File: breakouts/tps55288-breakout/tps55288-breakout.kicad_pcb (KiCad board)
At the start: 2 copper layers, 1 part, among them U1 TPS55288RPMR

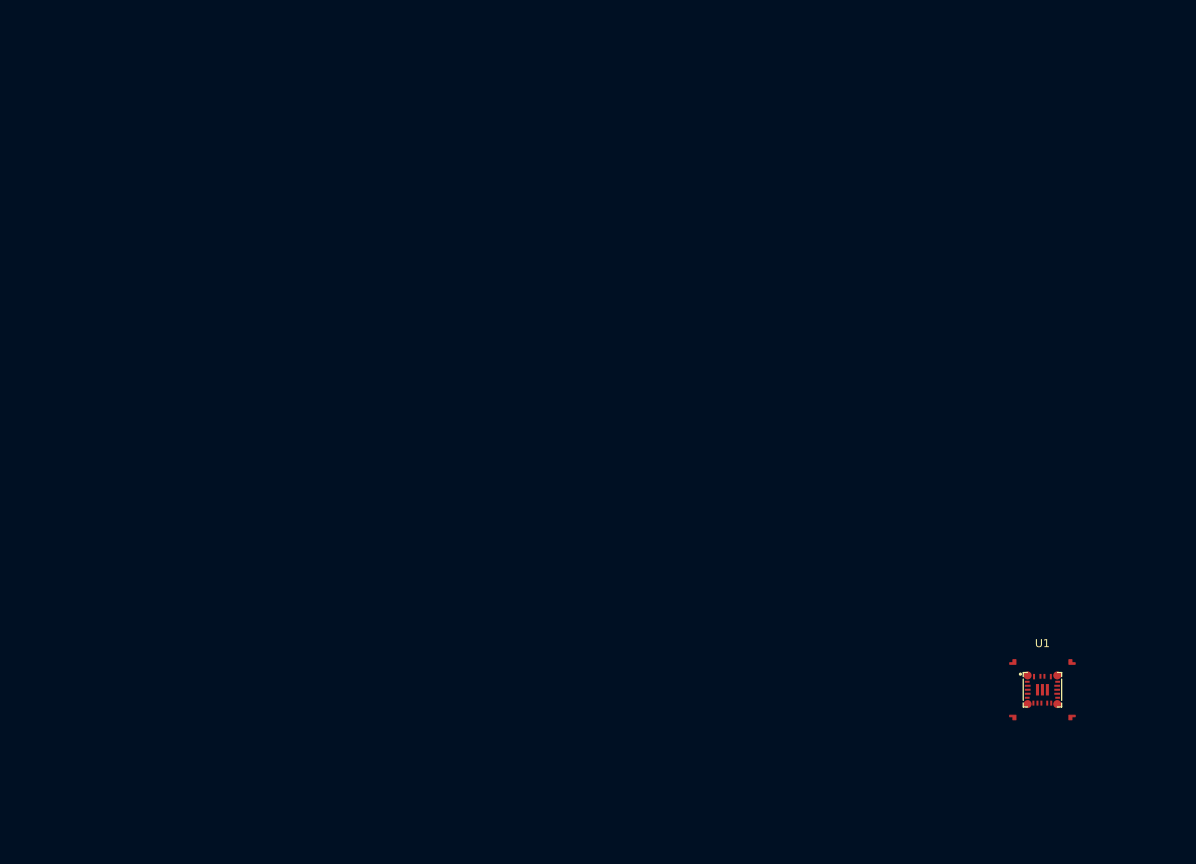
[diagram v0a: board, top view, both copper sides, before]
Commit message: finish schematic equations... by using the calculator that TI provides
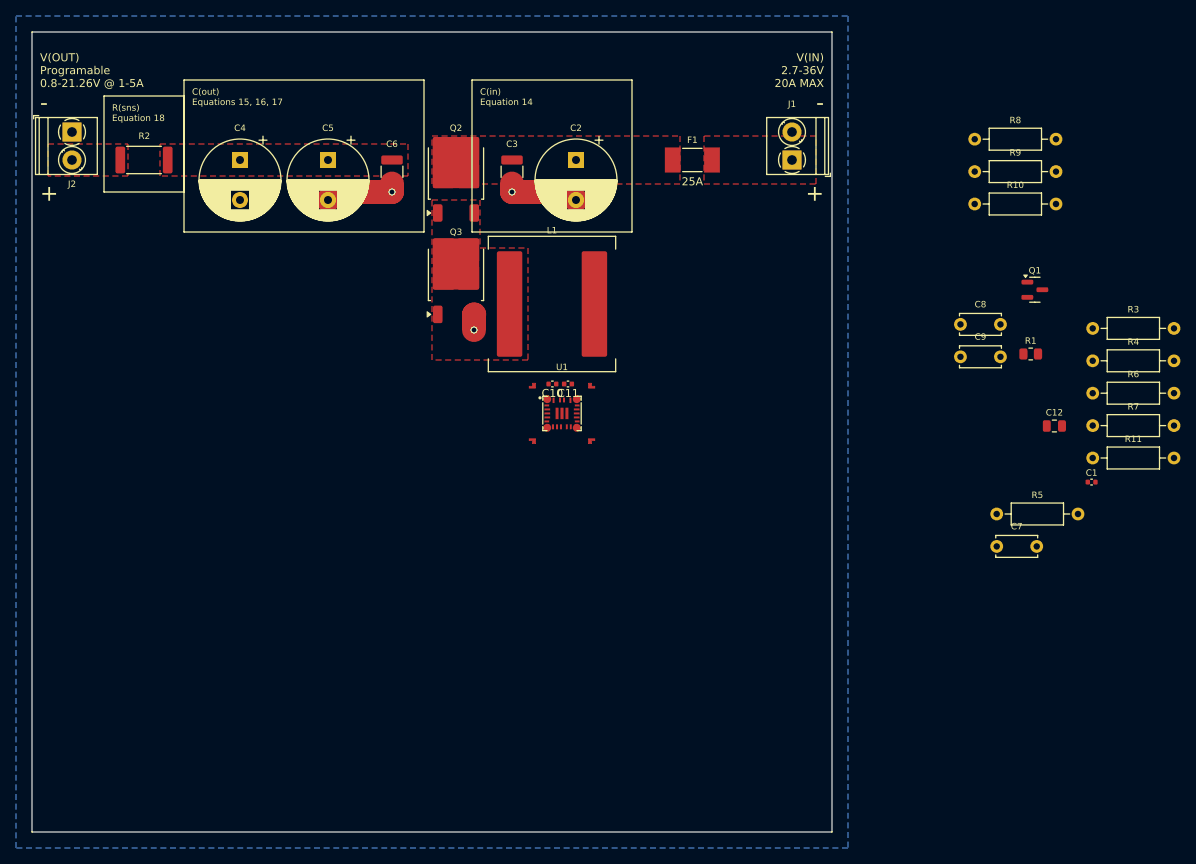
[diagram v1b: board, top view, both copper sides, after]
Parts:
- added C1: 0.1u, Capacitor_SMD:C_0402_1005Metric, F.Cu at (147.4, 71.3)
- added C10: 0.1u, Capacitor_SMD:C_0402_1005Metric, F.Cu at (80.0, 59.0)
- added C11: 0.1u, Capacitor_SMD:C_0402_1005Metric, F.Cu at (82.0, 59.0)
- added C12: 4.7u, Capacitor_SMD:C_0805_2012Metric, F.Cu at (142.8, 64.2)
- added C2: 330u, Capacitor_THT:CP_Radial_D10.0mm_P5.00mm, F.Cu at (83.0, 31.0)
- added C3: 10u, Capacitor_SMD:C_1210_3225Metric, F.Cu at (75.0, 32.5)
- added C4: 330u, Capacitor_THT:CP_Radial_D10.0mm_P5.00mm, F.Cu at (41.0, 31.0)
- added C5: 330u, Capacitor_THT:CP_Radial_D10.0mm_P5.00mm, F.Cu at (52.0, 31.0)
- added C6: 10u, Capacitor_SMD:C_1210_3225Metric, F.Cu at (60.0, 32.5)
- added C7: 10n, Capacitor_THT:C_Disc_D5.0mm_W2.5mm_P5.00mm, F.Cu at (135.6, 79.3)
- added C8: 150p, Capacitor_THT:C_Disc_D5.0mm_W2.5mm_P5.00mm, F.Cu at (131.1, 51.5)
- added C9: 15n, Capacitor_THT:C_Disc_D5.0mm_W2.5mm_P5.00mm, F.Cu at (131.1, 55.6)
- added F1: 25A, Fuse:Fuse_Littelfuse-NANO2-451_453, F.Cu at (97.5, 31.0)
- added J1: Screw_Terminal_01x02, TerminalBlock_Phoenix:TerminalBlock_Phoenix_PT-1,5-2-3.5-H_1x02_P3.50mm_Horizontal, F.Cu at (110.0, 31.0)
- added J2: Screw_Terminal_01x02, TerminalBlock_Phoenix:TerminalBlock_Phoenix_PT-1,5-2-3.5-H_1x02_P3.50mm_Horizontal, F.Cu at (20.0, 27.5)
- added L1: 4.7u, Inductor_SMD:L_Coilcraft_XAL1510-682, F.Cu at (80.0, 49.0)
- added Q1: 2N7002K, Package_TO_SOT_SMD:SOT-23, F.Cu at (140.4, 47.2)
- added Q2: QM6006D, Package_TO_SOT_SMD:TO-252-2, F.Cu at (68.0, 32.6)
- added Q3: QM6006D, Package_TO_SOT_SMD:TO-252-2, F.Cu at (68.0, 45.3)
- added R1: 10k, Resistor_SMD:R_0805_2012Metric, F.Cu at (139.8, 55.2)
- added R10: 16k, Resistor_THT:R_Axial_DIN0207_L6.3mm_D2.5mm_P10.16mm_Horizontal, F.Cu at (132.8, 36.5)
- added R11: 91k, Resistor_THT:R_Axial_DIN0207_L6.3mm_D2.5mm_P10.16mm_Horizontal, F.Cu at (147.6, 68.2)
- added R2: 10m, Resistor_SMD:R_2512_6332Metric, F.Cu at (29.0, 31.0)
- added R3: 4.3k, Resistor_THT:R_Axial_DIN0207_L6.3mm_D2.5mm_P10.16mm_Horizontal, F.Cu at (147.6, 52.0)
- added R4: 1k, Resistor_THT:R_Axial_DIN0207_L6.3mm_D2.5mm_P10.16mm_Horizontal, F.Cu at (147.6, 56.1)
- added R5: 47k, Resistor_THT:R_Axial_DIN0207_L6.3mm_D2.5mm_P10.16mm_Horizontal, F.Cu at (135.6, 75.2)
- added R6: 100k, Resistor_THT:R_Axial_DIN0207_L6.3mm_D2.5mm_P10.16mm_Horizontal, F.Cu at (147.6, 60.1)
- added R7: 1k, Resistor_THT:R_Axial_DIN0207_L6.3mm_D2.5mm_P10.16mm_Horizontal, F.Cu at (147.6, 64.2)
- added R8: 0, Resistor_THT:R_Axial_DIN0207_L6.3mm_D2.5mm_P10.16mm_Horizontal, F.Cu at (132.8, 28.4)
- added R9: 20k, Resistor_THT:R_Axial_DIN0207_L6.3mm_D2.5mm_P10.16mm_Horizontal, F.Cu at (132.8, 32.5)
- U1: footprint LCSC:VQFN-HR-26_L4.0-W3.5_TPS55288RPMR -> LCSC-powercoop:VQFN-HR-26_L4.0-W3.5_TPS55288RPMR
- moved U1 69.3 mm to (81.2, 62.7)
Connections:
- U1 pad 1: unconnected-(U1-DR1L-Pad1) -> /DR1L
- U1 pad 10: unconnected-(U1-AGND-Pad10) -> /AGND
- U1 pad 11: unconnected-(U1-VOUT-Pad11) -> /VOUT
- U1 pad 12: unconnected-(U1-ISP-Pad12) -> /VOUT
- U1 pad 13: unconnected-(U1-ISN-Pad13) -> /ISN
- U1 pad 14: unconnected-(U1-FB/INT-Pad14) -> /FB/INT
- U1 pad 15: unconnected-(U1-MODE-Pad15) -> /MODE
- U1 pad 16: unconnected-(U1-CDC-Pad16) -> /CDC
- U1 pad 17: unconnected-(U1-ILIM-Pad17) -> /ILIM
- U1 pad 18: unconnected-(U1-COMP-Pad18) -> /COMP
- U1 pad 19: unconnected-(U1-VCC-Pad19) -> /VCC
- U1 pad 2: unconnected-(U1-DR1H-Pad2) -> /DR1H
- U1 pad 20: unconnected-(U1-BOOT2-Pad20) -> /BOOT2
- U1 pad 21: unconnected-(U1-SW2-Pad21) -> /SW2
- U1 pad 22: unconnected-(U1-BOOT1-Pad22) -> /BOOT1
- U1 pad 23: unconnected-(U1-SW1-Pad23) -> /SW1
- U1 pad 24: unconnected-(U1-PGND-Pad24) -> GND
- U1 pad 25: unconnected-(U1-SW2-Pad25) -> /SW2
- U1 pad 26: unconnected-(U1-VOUT-Pad26) -> /VOUT
- U1 pad 3: unconnected-(U1-VIN-Pad3) -> /VIN
- U1 pad 4: unconnected-(U1-EN/UVLO-Pad4) -> /EN/UVLO
- U1 pad 5: unconnected-(U1-SCL-Pad5) -> /SCL
- U1 pad 6: unconnected-(U1-SDA-Pad6) -> /SDA
- U1 pad 7: unconnected-(U1-DITH/SYNC-Pad7) -> /DITH/SYNC
- U1 pad 8: unconnected-(U1-FSW-Pad8) -> /FSW
- U1 pad 9: unconnected-(U1-PGND-Pad9) -> GND
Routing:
- net GND: track 0.00 -> 20.9 mm, vias 0 -> 3
- added copper zone on F.Cu, net /ISN
- added copper zone on F.Cu, net /SW1
- added copper zone on F.Cu, net /VIN
- added copper zone on F.Cu, net /VOUT
- added copper zone on B.Cu, net GND
- added copper zone on F.Cu, net Net-(J1-Pin_1)
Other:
- board outline added: 100 x 100 mm
- board text added: "+"
- board text added: "-"
- board text added: "C(in) Equation 14"
- board text added: "C(out) Equations 15, 16, 17"
- board text added: "R(sns) Equation 18"
- board text added: "V(IN) 2.7-36V 20A MAX"
- board text added: "V(OUT) Programable 0.8-21.26V @ 1-5A"

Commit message: first pass at full-featured TPS55288 breakout board
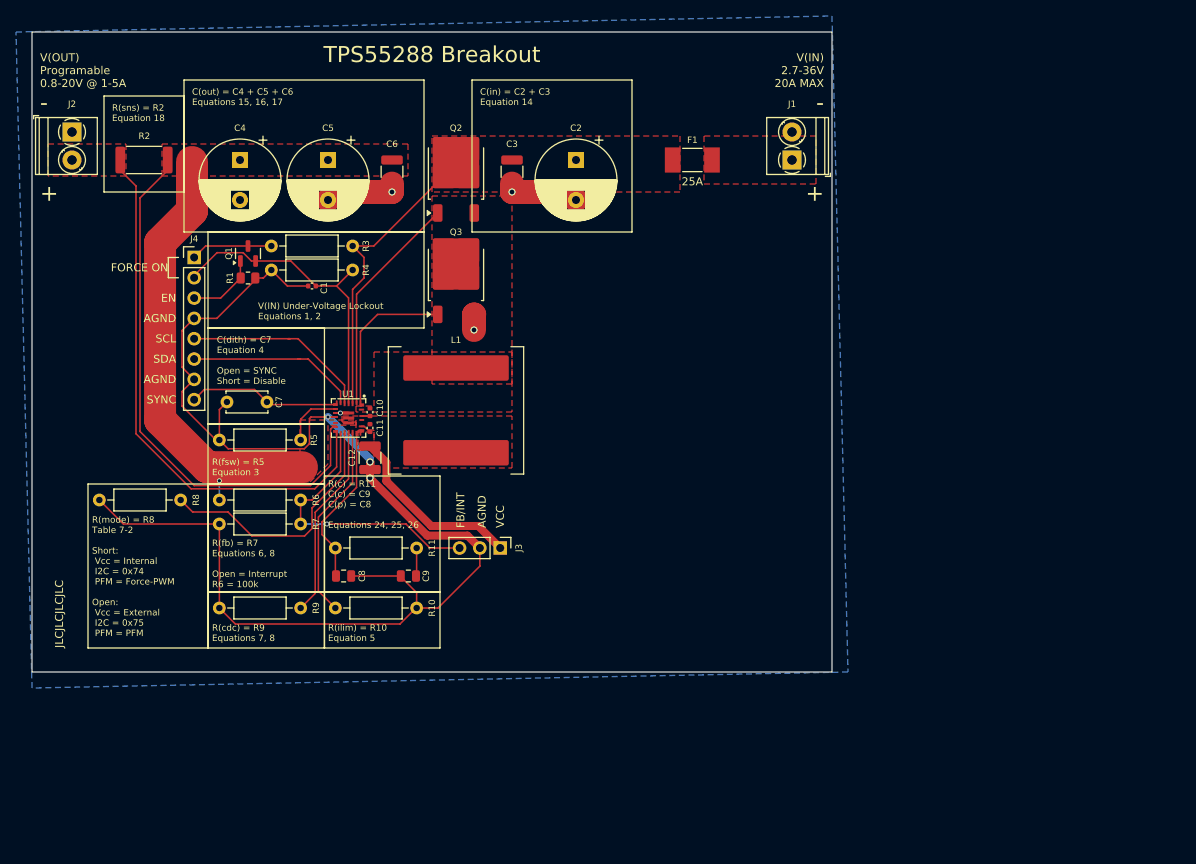
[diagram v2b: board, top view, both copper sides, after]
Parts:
- added J3: Conn_01x10_Pin, Connector_PinHeader_2.54mm:PinHeader_1x03_P2.54mm_Vertical, F.Cu at (73.5, 79.5)
- added J4: Conn_01x06_Pin, Connector_PinHeader_2.54mm:PinHeader_1x08_P2.54mm_Vertical, F.Cu at (35.3, 43.2)
- C12: value 4.7u -> 10u; footprint Capacitor_SMD:C_0805_2012Metric -> Capacitor_SMD:C_1210_3225Metric
- C2: value 330u -> 100u
- C8, C9: footprint Capacitor_THT:C_Disc_D5.0mm_W2.5mm_P5.00mm -> Capacitor_SMD:C_0805_2012Metric
- moved R6 110.0 mm to (38.4, 73.5)
- moved R8 109.0 mm to (33.6, 73.5), turned to 180 degrees
- moved C1 100.5 mm to (50.0, 46.8)
- moved R9 100.4 mm to (48.6, 87.0), turned to 180 degrees
- moved R7 99.8 mm to (48.6, 76.5), turned to 180 degrees
- moved Q1 98.5 mm to (42.0, 42.7), turned to 90 degrees
- moved R1 98.3 mm to (42.0, 45.8), turned to 180 degrees
- moved C7 97.9 mm to (39.4, 61.2)
- moved R11 95.3 mm to (52.9, 79.5)
- moved R10 94.5 mm to (52.9, 87.0)
- moved R4 93.2 mm to (55.1, 44.8), turned to 180 degrees
- moved R3 93.1 mm to (55.1, 41.8), turned to 180 degrees
- moved R5 87.5 mm to (48.6, 66.0), turned to 180 degrees
- moved C12 85.6 mm to (57.2, 68.2), turned to 90 degrees
- moved C8 83.3 mm to (54.0, 83.0), turned to 180 degrees
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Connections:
- net Net-(Q1-D) renamed /ON
- C7 pad 1: GND -> /AGND
- Q1 pad 2: Net-(Q1-S) -> /EN/UVLO
- R5 pad 2: GND -> /AGND
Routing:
- net /AGND: track 0.00 -> 164.2 mm, vias 0 -> 2
- net /VOUT: track 0.00 -> 124.8 mm, vias 0 -> 1
- net /ISN: track 0.00 -> 68.7 mm
- net /EN/UVLO: track 0.00 -> 38.8 mm
- net /VIN: track 0.00 -> 35.9 mm
- net /FB/INT: track 0.00 -> 35.4 mm, vias 0 -> 1
- net /MODE: track 0.00 -> 32.3 mm
- net /DR1H: track 0.00 -> 27.9 mm
- net /ILIM: track 0.00 -> 24.6 mm
- net /CDC: track 0.00 -> 24.4 mm
- net /SCL: track 0.00 -> 23.8 mm
- net /VCC: track 0.00 -> 22.9 mm
- net /SDA: track 0.00 -> 21.7 mm
- net /COMP: track 0.00 -> 20.4 mm
- net /DR1L: track 0.00 -> 19.5 mm
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- added copper zone on F.Cu, net /SW2
- added copper zone on F.Cu, net /VCC
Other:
- board size 100 x 100 mm -> 100 x 80 mm
- board text added: "AGND"
- board text added: "C(dith) = C7 Equation 4 Open = SYNC Short = Disable"
- board text added: "C(in) = C2 + C3 Equation 14"
- board text added: "C(out) = C4 + C5 + C6 Equations 15, 16, 17"
- board text added: "EN"
- board text added: "FB/INT"
- board text added: "FORCE ON"
- board text added: "JLCJLCJLCJLC"
- board text added: "R(c) = R11 C(c) = C9 C(p) = C8 Equations 24, 25, 26"
- board text added: "R(cdc) = R9 Equations 7, 8"
- board text added: "R(fb) = R7 Equations 6, 8 Open = Interrupt R6 = 100k"
- board text added: "R(fsw) = R5 Equation 3"
- board text added: "R(ilim) = R10 Equation 5"
- board text added: "R(mode) = R8 Table 7-2 Short: Vcc = Internal I2C = 0x74 PFM = Force-PWM Open: Vcc = External I2C = 0x75 PFM = PFM"
- board text added: "R(sns) = R2 Equation 18"
- board text added: "SCL"
- board text added: "SDA"
- board text added: "SYNC"
- board text added: "TPS55288 Breakout"
- board text added: "V(IN) Under-Voltage Lockout Equations 1, 2"
- board text added: "V(OUT) Programable 0.8-20V @ 1-5A"
- board text added: "VCC"
- board text removed: "C(in) Equation 14"
- board text removed: "C(out) Equations 15, 16, 17"
- board text removed: "R(sns) Equation 18"
- board text removed: "V(OUT) Programable 0.8-21.26V @ 1-5A"

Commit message: prototype board updates - add many silkscreen things
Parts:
- added JP1: SolderJumper_2_Bridged, Jumper:SolderJumper-2_P1.3mm_Bridged2Bar_Pad1.0x1.5mm, B.Cu at (57.2, 69.5)
- F1: value 25A -> 20A
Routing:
- net GND: vias 5 -> 4
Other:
- board text added: "C(c)="
- board text added: "C(dith)="
- board text added: "C(in) = C2 + C3 Equation 14 Use 50V Rated Capacitors"
- board text added: "C(in)="
- board text added: "C(out) = C4 + C5 + C6 Equations 15, 16, 17 Use 25V Rated Capacitors"
- board text added: "C(out)="
- board text added: "C(p)="
- board text added: "Design (C) Joel Michael, 2025 For the PowerCoop Project"
- board text added: "LUMP OF COPPER"
- board text added: "LittleFuse NANO2 0453020. OR SIMILAR"
- board text added: "R(c)="
- board text added: "R(cdc)="
- board text added: "R(fb)="
- board text added: "R(fsw)="
- board text added: "R(ilim)="
- board text added: "R(mode)="
- board text added: "R(sns)="
- board text added: "S/N:"
- board text added: "TPS55288 Prototyping Board"
- board text added: "V(IN) UVLO="
- board text removed: "C(in) = C2 + C3 Equation 14"
- board text removed: "C(out) = C4 + C5 + C6 Equations 15, 16, 17"
- board text removed: "TPS55288 Breakout"
